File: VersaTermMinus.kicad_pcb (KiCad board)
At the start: 2 copper layers, 83.5 x 77.7 mm, 55 parts, among them CN1 HDMI_A, CN2 DE15_Socket, CN3 USB_B_Micro, CN5 USB_B_Micro, CN6 Mini-DIN-6, CN7 TTL Serial, CN8 DE9 Socket, J2 USBDATA, Q1 2N7002, Q2 2N7002, Q3 2N7002, Q4 2N7002AK, Q5 2N7002, Q6 2N7002, Q7 2N7002, SW1 RESET, SW2 DEFAULTS, SW3 3V3/5V, U1 Raspberry Pi Pico, U3 MAX3232

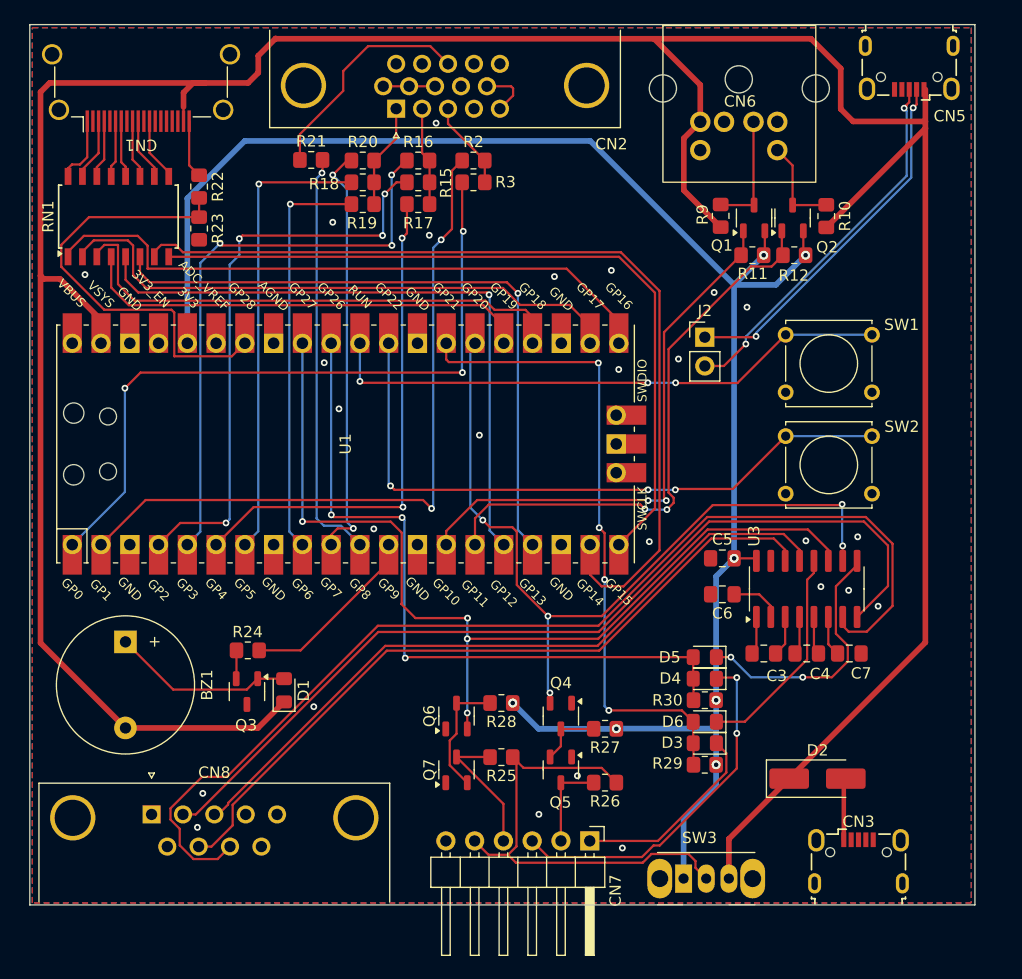
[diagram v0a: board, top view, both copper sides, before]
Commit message: add silkscreen labelling
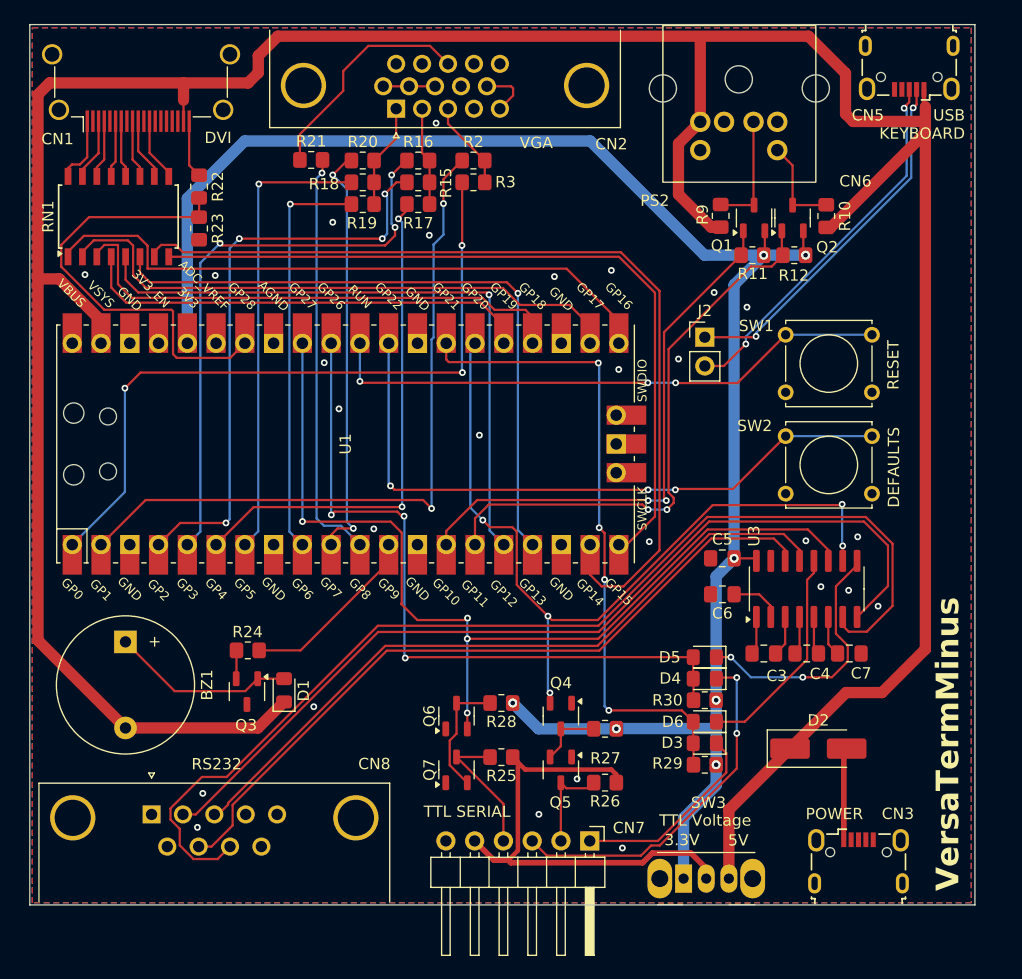
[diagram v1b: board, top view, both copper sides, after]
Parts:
- moved D2 2.65 mm to (127.8, 113.5)
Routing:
- net Net-(CN3-VBUS): track 5.47 -> 8.15 mm
- net +3.3V: track 159.2 -> 157.0 mm
- net VTTL: track 42.0 -> 43.2 mm
- net GND: vias 26 -> 27
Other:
- board text added: "3.3V"
- board text added: "5V"
- board text added: "DEFAULTS"
- board text added: "DVI"
- board text added: "POWER"
- board text added: "PS2"
- board text added: "RESET"
- board text added: "RS232"
- board text added: "TTL SERIAL"
- board text added: "TTL Voltage"
- board text added: "USB KEYBOARD"
- board text added: "VGA"
- board text added: "VersaTermMinus"
- board text added: "https://github.com/dhansel/VersaTerm"
- board text added: "https://github.com/jimbro1000/VersaTermMinus"

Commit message: update fields on pcb
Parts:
- Q1, Q2, Q3, Q5, Q6, Q7: value 2N7002 -> 2N7002AK
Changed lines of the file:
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@@
 			)
 		)
-		(property "Value" "2N7002"
+		(property "Value" "2N7002AK"
 			(at 0 2.4 -90)
 			(layer "F.Fab")
@@
 			)
 		)
+		(property "DigiKey" "1N4148WXTPMSCT-ND"
+			(at 0 0 90)
+			(unlocked yes)
+			(layer "F.Fab")
+			(hide yes)
+			(effects
+				(font
+					(size 1 1)
+					(thickness 0.15)
+				)
+			)
+		)
 		(property ki_fp_filters "D*DO?35*")
 		(sheetname "Root")
@@
 			)
 		)
+		(property "DigiKey" "609-4614-1-ND"
+			(at 0 0 180)
+			(unlocked yes)
+			(layer "F.Fab")
+			(hide yes)
+			(effects
+				(font
+					(size 1 1)
+					(thickness 0.15)
+				)
+			)
+		)
 		(property ki_fp_filters "HDMI*A*")
 		(sheetname "Root")
@@
 			)
 		)
+		(property "DigiKey" "1N4148WXTPMSCT-ND"
+			(at 0 0 180)
+			(unlocked yes)
+			(layer "F.Fab")
+			(hide yes)
+			(effects
+				(font
+					(size 1 1)
+					(thickness 0.15)
+				)
+			)
+		)
 		(property ki_fp_filters "D*DO?35*")
 		(sheetname "Root")
@@
 			)
 		)
-		(property "Value" "2N7002"
+		(property "Value" "2N7002AK"
 			(at 0 2.4 -90)
 			(layer "F.Fab")
@@
 			)
 		)
+		(property "DigiKey" "4816P-1-271LFCT-ND"
+			(at 0 0 90)
+			(unlocked yes)
+			(layer "F.Fab")
+			(hide yes)
+			(effects
+				(font
+					(size 1 1)
+					(thickness 0.15)
+				)
+			)
+		)
 		(property ki_fp_filters "DIP* SOIC* R*Array*Concave* R*Array*Convex*")
 		(sheetname "Root")
@@
 			)
 		)
+		(property "DigiKey" "AE10968-ND"
+			(at 0 0 0)
+			(unlocked yes)
+			(layer "F.Fab")
+			(hide yes)
+			(effects
+				(font
+					(size 1 1)
+					(thickness 0.15)
+				)
+			)
+		)
 		(property ki_fp_filters "DSUB*Female*")
 		(sheetname "Root")
@@
 			)
 		)
+		(property "DigiKey" "450-1157-ND"
+			(at 0 0 0)
+			(unlocked yes)
+			(layer "F.Fab")
+			(hide yes)
+			(effects
+				(font
+					(size 1 1)
+					(thickness 0.15)
+				)
+			)
+		)
 		(sheetname "Root")
 		(sheetfile "VersaTermMinus.kicad_sch")
@@
 			)
 		)
+		(property "DigiKey" "1N4148WXTPMSCT-ND"
+			(at 0 0 180)
+			(unlocked yes)
+			(layer "F.Fab")
+			(hide yes)
+			(effects
+				(font
+					(size 1 1)
+					(thickness 0.15)
+				)
+			)
+		)
 		(property ki_fp_filters "D*DO?35*")
 		(sheetname "Root")
@@
 			)
 		)
+		(property "DigiKey" "1N4148WXTPMSCT-ND"
+			(at 0 0 180)
+			(unlocked yes)
+			(layer "F.Fab")
+			(hide yes)
+			(effects
+				(font
+					(size 1 1)
+					(thickness 0.15)
+				)
+			)
+		)
 		(property ki_fp_filters "D*DO?35*")
 		(sheetname "Root")
@@
 			)
 		)
-		(property "Value" "2N7002"
+		(property "Value" "2N7002AK"
 			(at 0 2.4 -90)
 			(layer "F.Fab")
@@
 			)
 		)
-		(property "Value" "2N7002"
+		(property "Value" "2N7002AK"
 			(at 0 2.4 90)
 			(layer "F.Fab")
@@
 			)
 		)
+		(property "DigiKey" "L77HDE15SD1CH4FVGA-ND"
+			(at 0 0 180)
+			(unlocked yes)
+			(layer "F.Fab")
+			(hide yes)
+			(effects
+				(font
+					(size 1 1)
+					(thickness 0.15)
+				)
+			)
+		)
 		(property ki_fp_filters "DSUB*Female*")
 		(sheetname "Root")
@@
 			)
 		)
+		(property "DigiKey" "450-1157-ND"
+			(at 0 0 0)
+			(unlocked yes)
+			(layer "F.Fab")
+			(hide yes)
+			(effects
+				(font
+					(size 1 1)
+					(thickness 0.15)
+				)
+			)
+		)
 		(sheetname "Root")
 		(sheetfile "VersaTermMinus.kicad_sch")
@@
 			)
 		)
+		(property "DigiKey" "641-1762-1-ND"
+			(at 0 0 0)
+			(unlocked yes)
+			(layer "F.Fab")
+			(hide yes)
+			(effects
+				(font
+					(size 1 1)
+					(thickness 0.15)
+				)
+			)
+		)
 		(property ki_fp_filters "TO-???* *_Diode_* *SingleDiode* D_*")
 		(sheetname "Root")
@@
 			)
 		)
+		(property "DigiKey" "732-5960-1-ND"
+			(at 0 0 180)
+			(unlocked yes)
+			(layer "F.Fab")
+			(hide yes)
+			(effects
+				(font
+					(size 1 1)
+					(thickness 0.15)
+				)
+			)
+		)
 		(property ki_fp_filters "USB*")
 		(sheetname "Root")
@@
 			)
 		)
-		(property "Value" "2N7002"
+		(property "Value" "2N7002AK"
 			(at 0 2.4 90)
 			(layer "F.Fab")
@@
 			)
 		)
+		(property "DigiKey" "1N4148WXTPMSCT-ND"
+			(at 0 0 180)
+			(unlocked yes)
+			(layer "F.Fab")
+			(hide yes)
+			(effects
+				(font
+					(size 1 1)
+					(thickness 0.15)
+				)
+			)
+		)
 		(property ki_fp_filters "D*DO?35*")
 		(sheetname "Root")
@@
 			)
 		)
-		(property "Value" "2N7002"
+		(property "Value" "2N7002AK"
 			(at 0 2.4 -90)
 			(layer "F.Fab")
@@
 			)
 		)
+		(property "DigiKey" "CKN9559-ND"
+			(at 0 0 0)
+			(unlocked yes)
+			(layer "F.Fab")
+			(hide yes)
+			(effects
+				(font
+					(size 1 1)
+					(thickness 0.15)
+				)
+			)
+		)
 		(sheetname "Root")
 		(sheetfile "VersaTermMinus.kicad_sch")
@@
 				)
 			)
+		)
+		(property "DigiKey" "732-5960-1-ND"
+			(at 0 0 0)
+			(unlocked yes)
+			(layer "F.Fab")
+			(hide yes)
+			(effects
+				(font
+					(size 1 1)
+					(thickness 0.15)
+				)
+			)

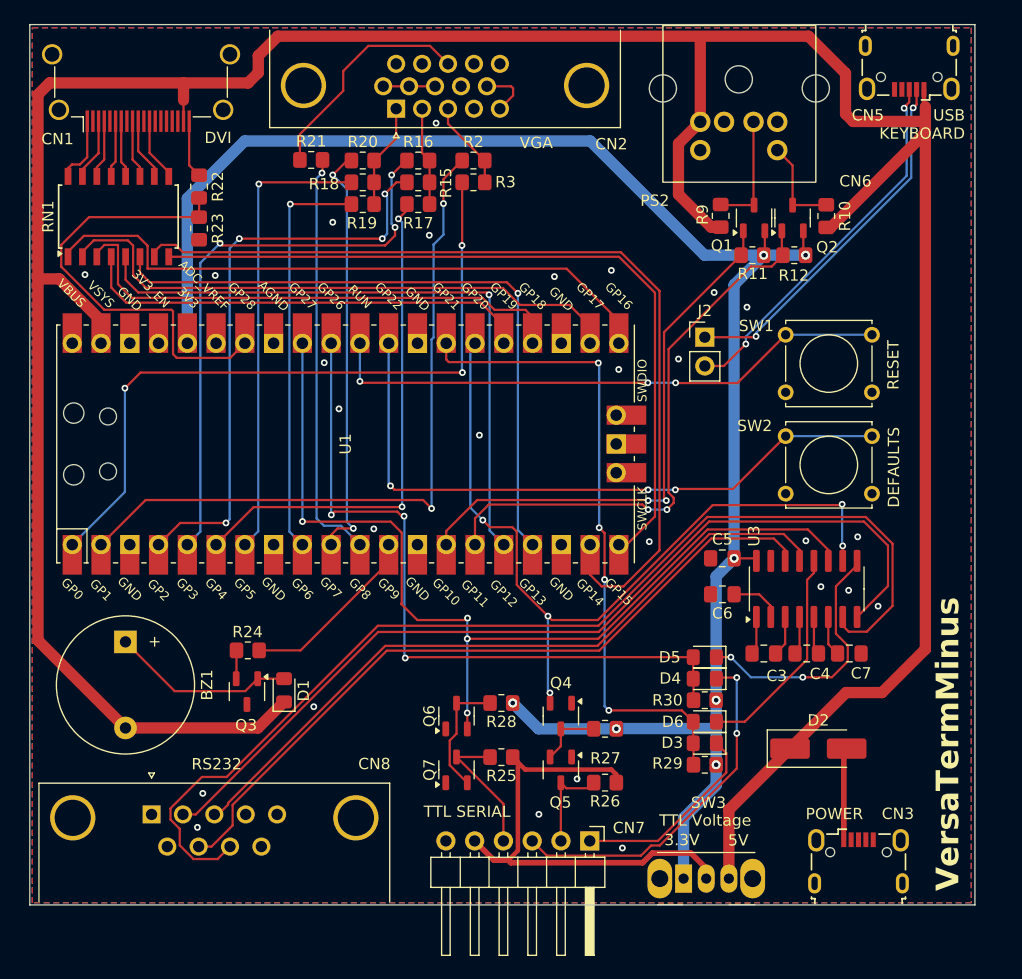
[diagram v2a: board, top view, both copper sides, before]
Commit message: fix de9 and buzzer
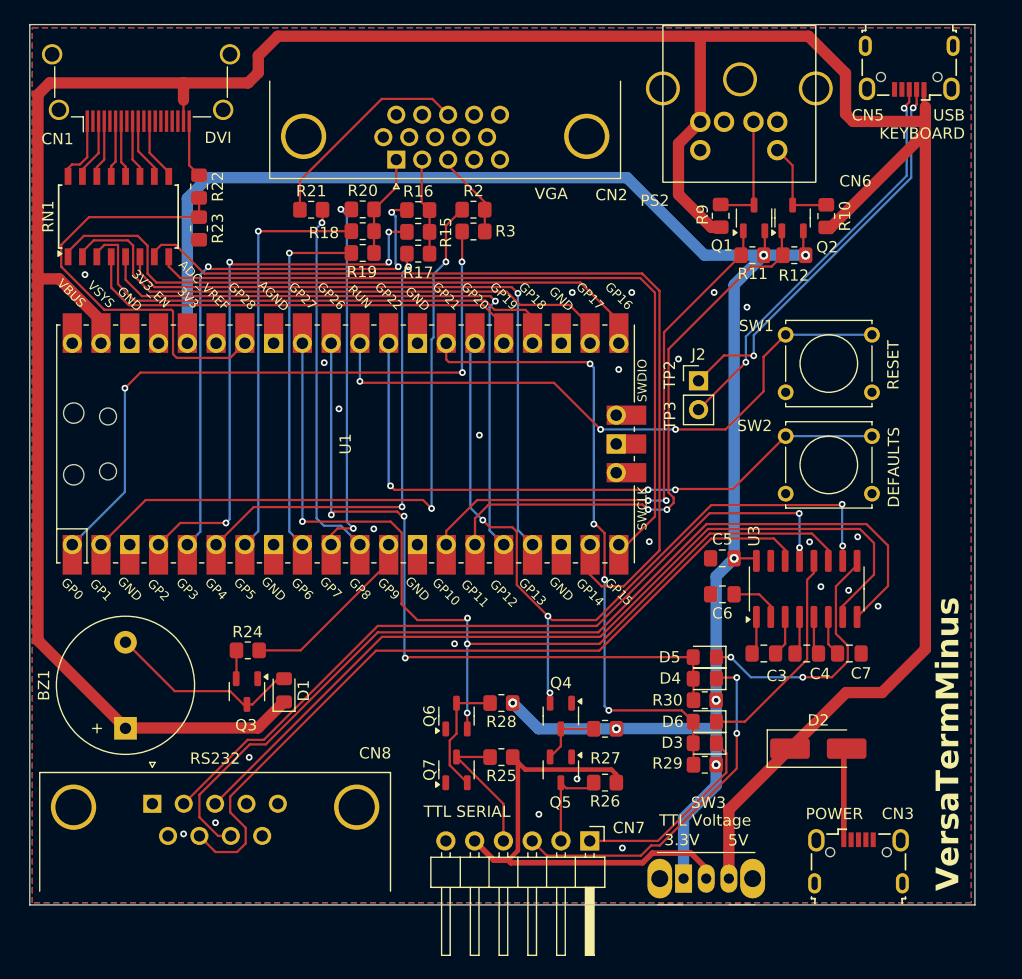
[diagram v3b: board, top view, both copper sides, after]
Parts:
- Q1, Q2, Q3, Q5, Q6, Q7: value 2N7002AK -> 2N7002
- moved BZ1 7.63 mm to (66.7, 111.7), turned to 90 degrees
- moved CN2 4.49 mm to (90.6, 61.5)
- moved R21 4.40 mm to (83.0, 65.9)
- moved R16 4.37 mm to (92.5, 65.9)
- moved R15 4.37 mm to (92.5, 67.8)
- moved R17 4.37 mm to (92.5, 69.8)
- moved R2 4.34 mm to (97.4, 65.9)
- moved R3 4.34 mm to (97.4, 67.8)
- moved R20 4.31 mm to (87.6, 65.9)
- moved R18 4.31 mm to (87.6, 67.8)
- moved R19 4.31 mm to (87.6, 69.7)
- moved J2 3.89 mm to (117.2, 81.0)
- moved CN8 0.94 mm to (69.0, 118.3)
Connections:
- BZ1 pad 1: Net-(BZ1-+) -> +5V
- BZ1 pad 2: +5V -> Net-(BZ1--)
- CN8 pad 2: Net-(U3-R2IN) -> Net-(U3-R1IN)
- CN8 pad 3: Net-(U3-R1IN) -> Net-(U3-T2OUT)
- CN8 pad 8: Net-(U3-T2OUT) -> Net-(U3-R2IN)
- D1 pad 2: Net-(BZ1-+) -> Net-(BZ1--)
- Q3 pad 1: Net-(BZ1-+) -> GND
- Q3 pad 3: GND -> Net-(BZ1--)
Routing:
- net Net-(U3-T2OUT): track 96.2 -> 76.4 mm
- net Net-(BZ1--): track 0.00 -> 17.2 mm
- net Net-(BZ1-+): track 16.3 -> 0.00 mm
- net GND: track 9.25 -> 0.00 mm, vias 27 -> 24
- net Net-(U3-R1IN): track 63.6 -> 69.2 mm, vias 0 -> 2
- net RESET: track 50.4 -> 55.6 mm
- net R2: track 37.2 -> 32.6 mm
- net G2: track 45.1 -> 40.6 mm
- net SYNC: track 36.7 -> 32.3 mm
- net B1: track 63.0 -> 58.6 mm
- net B0: track 62.9 -> 58.6 mm
- net R1: track 36.0 -> 31.7 mm
- net R0: track 40.6 -> 36.4 mm
- net Net-(U3-T1OUT): track 65.5 -> 69.5 mm
- net G0: track 51.5 -> 48.4 mm
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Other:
- board text added: "TP2"
- board text added: "TP3"

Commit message: populate missing BOM fields
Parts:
- Q4: value 2N7002AK -> 2N7002
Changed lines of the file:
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@@
 			)
 		)
+		(property "DigiKey" "1N4148WXTPMSCT-ND"
+			(at 0 0 90)
+			(unlocked yes)
+			(layer "F.Fab")
+			(hide yes)
+			(effects
+				(font
+					(size 1 1)
+					(thickness 0.15)
+				)
+			)
+		)
 		(property ki_fp_filters "D*DO?35*")
 		(sheetname "Root")
@@
 			)
 		)
+		(property "DigiKey" "609-4614-1-ND"
+			(at 0 0 180)
+			(unlocked yes)
+			(layer "F.Fab")
+			(hide yes)
+			(effects
+				(font
+					(size 1 1)
+					(thickness 0.15)
+				)
+			)
+		)
 		(property ki_fp_filters "HDMI*A*")
 		(sheetname "Root")
@@
 			)
 		)
+		(property "DigiKey" "1N4148WXTPMSCT-ND"
+			(at 0 0 180)
+			(unlocked yes)
+			(layer "F.Fab")
+			(hide yes)
+			(effects
+				(font
+					(size 1 1)
+					(thickness 0.15)
+				)
+			)
+		)
 		(property ki_fp_filters "D*DO?35*")
 		(sheetname "Root")
@@
 			)
 		)
-		(property "Datasheet" ""
+		(property "Datasheet" "https://www.bourns.com/docs/Product-Datasheets/4800P.pdf"
 			(at 0 0 90)
 			(unlocked yes)
@@
 			)
 		)
+		(property "DigiKey" "4816P-1-271LFCT-ND"
+			(at 0 0 90)
+			(unlocked yes)
+			(layer "F.Fab")
+			(hide yes)
+			(effects
+				(font
+					(size 1 1)
+					(thickness 0.15)
+				)
+			)
+		)
 		(property ki_fp_filters "DIP* SOIC* R*Array*Concave* R*Array*Convex*")
 		(sheetname "Root")
@@
 			)
 		)
+		(property "DigiKey" "AE10968-ND"
+			(at 0 0 0)
+			(unlocked yes)
+			(layer "F.Fab")
+			(hide yes)
+			(effects
+				(font
+					(size 1 1)
+					(thickness 0.15)
+				)
+			)
+		)
 		(property ki_fp_filters "DSUB*Female*")
 		(sheetname "Root")
@@
 			)
 		)
-		(property "Datasheet" ""
+		(property "Datasheet" "https://www.ckswitches.com/media/1457/ksa_ksl.pdf"
 			(at 0 0 0)
 			(unlocked yes)
@@
 			)
 		)
+		(property "DigiKey" "CKN10734-ND"
+			(at 0 0 0)
+			(unlocked yes)
+			(layer "F.Fab")
+			(hide yes)
+			(effects
+				(font
+					(size 1 1)
+					(thickness 0.15)
+				)
+			)
+		)
 		(sheetname "Root")
 		(sheetfile "VersaTermMinus.kicad_sch")
@@
 			)
 		)
+		(property "DigiKey" "1N4148WXTPMSCT-ND"
+			(at 0 0 180)
+			(unlocked yes)
+			(layer "F.Fab")
+			(hide yes)
+			(effects
+				(font
+					(size 1 1)
+					(thickness 0.15)
+				)
+			)
+		)
 		(property ki_fp_filters "D*DO?35*")
 		(sheetname "Root")
@@
 			)
 		)
+		(property "DigiKey" "1N4148WXTPMSCT-ND"
+			(at 0 0 180)
+			(unlocked yes)
+			(layer "F.Fab")
+			(hide yes)
+			(effects
+				(font
+					(size 1 1)
+					(thickness 0.15)
+				)
+			)
+		)
 		(property ki_fp_filters "D*DO?35*")
 		(sheetname "Root")
@@
 			)
 		)
+		(property "DigiKey" "L77HDE15SD1CH4FVGA-ND"
+			(at 0 0 180)
+			(unlocked yes)
+			(layer "F.Fab")
+			(hide yes)
+			(effects
+				(font
+					(size 1 1)
+					(thickness 0.15)
+				)
+			)
+		)
 		(property ki_fp_filters "DSUB*Female*")
 		(sheetname "Root")
@@
 			)
 		)
-		(property "Datasheet" ""
+		(property "Datasheet" "https://www.ckswitches.com/media/1457/ksa_ksl.pdf"
 			(at 0 0 0)
 			(unlocked yes)
@@
 			)
 		)
+		(property "DigiKey" "CKN10734-ND"
+			(at 0 0 0)
+			(unlocked yes)
+			(layer "F.Fab")
+			(hide yes)
+			(effects
+				(font
+					(size 1 1)
+					(thickness 0.15)
+				)
+			)
+		)
 		(sheetname "Root")
 		(sheetfile "VersaTermMinus.kicad_sch")
@@
 			)
 		)
-		(property "Value" "2N7002AK"
+		(property "Value" "2N7002"
 			(at 0 2.4 90)
 			(layer "F.Fab")
@@
 			)
 		)
+		(property "DigiKey" "641-1762-1-ND"
+			(at 0 0 0)
+			(unlocked yes)
+			(layer "F.Fab")
+			(hide yes)
+			(effects
+				(font
+					(size 1 1)
+					(thickness 0.15)
+				)
+			)
+		)
 		(property ki_fp_filters "TO-???* *_Diode_* *SingleDiode* D_*")
 		(sheetname "Root")
@@
 			)
 		)
-		(property "Datasheet" ""
+		(property "Datasheet" "https://www.we-online.com/katalog/datasheet/629105150521.pdf"
 			(at 0 0 180)
 			(unlocked yes)
@@
 			)
 		)
+		(property "DigiKey" "732-5960-1-ND"
+			(at 0 0 180)
+			(unlocked yes)
+			(layer "F.Fab")
+			(hide yes)
+			(effects
+				(font
+					(size 1 1)
+					(thickness 0.15)
+				)
+			)
+		)
 		(property ki_fp_filters "USB*")
 		(sheetname "Root")
@@
 			)
 		)
+		(property "DigiKey" "1N4148WXTPMSCT-ND"
+			(at 0 0 180)
+			(unlocked yes)
+			(layer "F.Fab")
+			(hide yes)
+			(effects
+				(font
+					(size 1 1)
+					(thickness 0.15)
+				)
+			)
+		)
 		(property ki_fp_filters "D*DO?35*")
 		(sheetname "Root")
@@
 			)
 		)
-		(property "Datasheet" ""
+		(property "Datasheet" "https://www.ckswitches.com/media/1428/os.pdf"
 			(at 0 0 0)
 			(unlocked yes)
@@
 			)
 		)
+		(property "DigiKey" "CKN9559-ND"
+			(at 0 0 0)
+			(unlocked yes)
+			(layer "F.Fab")
+			(hide yes)
+			(effects
+				(font
+					(size 1 1)
+					(thickness 0.15)
+				)
+			)
+		)
 		(sheetname "Root")
 		(sheetfile "VersaTermMinus.kicad_sch")
@@
 			)
 		)
-		(property "Datasheet" ""
+		(property "Datasheet" "https://www.we-online.com/katalog/datasheet/629105150521.pdf"
 			(at 0 0 0)
 			(unlocked yes)
@@
 					(thickness 0.15)
 				)
+			)
+		)
+		(property "DigiKey" "732-5960-1-ND"
+			(at 0 0 0)
+			(unlocked yes)
+			(layer "F.Fab")
+			(hide yes)
+			(effects
+				(font
+					(size 1 1)
+					(thickness 0.15)
+				)
